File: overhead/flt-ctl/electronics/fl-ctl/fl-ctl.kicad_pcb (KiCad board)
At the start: 2 copper layers, 145 x 47.3 mm, 31 parts, among them J1 Conn_02x01, J2 Conn_02x05_Counter_Clockwise

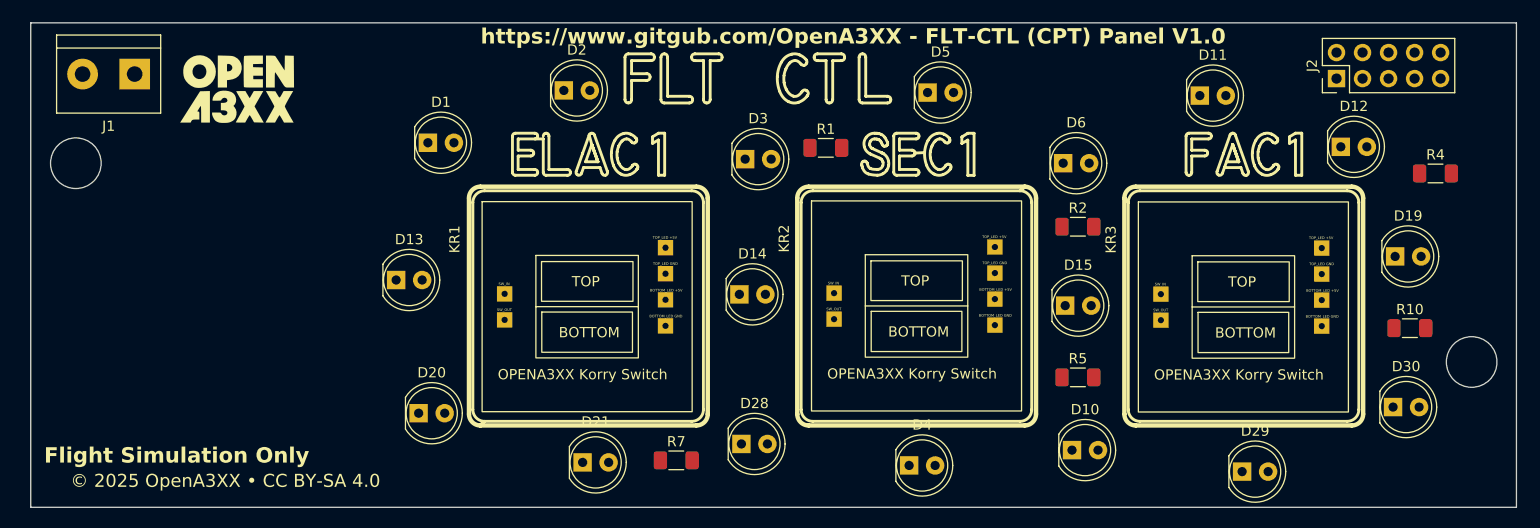
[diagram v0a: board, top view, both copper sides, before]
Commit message: Finalised ROuting for FLT-CTL CPT Side, and cleaned up ADIRS Panel PCB
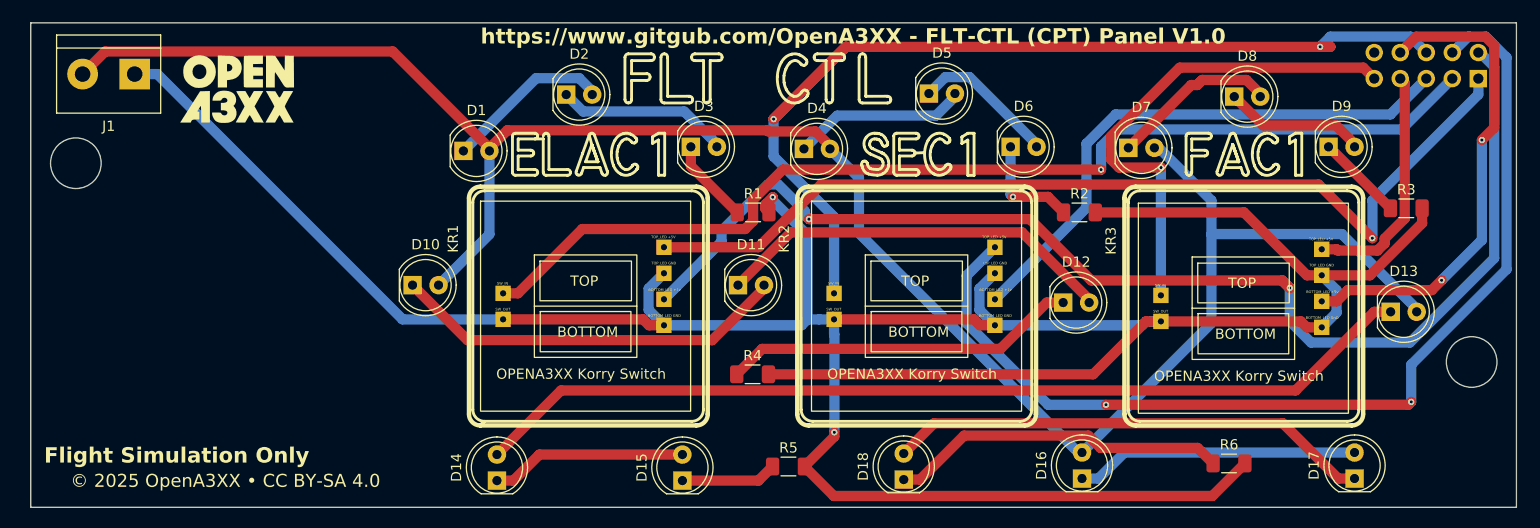
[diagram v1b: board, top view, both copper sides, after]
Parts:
- removed D19, D20, D21, D28, D29, D30: LED, LED_THT:LED_D5.0mm_Clear
- removed R10, R7: 220R, Resistor_SMD:R_1206_3216Metric_Pad1.30x1.75mm_HandSolder
- added D16: LED, LED_THT:LED_D5.0mm_Clear, F.Cu at (177.3, 121.4)
- added D17: LED, LED_THT:LED_D5.0mm_Clear, F.Cu at (203.9, 121.4)
- added D18: LED, LED_THT:LED_D5.0mm_Clear, F.Cu at (159.9, 121.5)
- added D7: LED, LED_THT:LED_D5.0mm_Clear, F.Cu at (181.8, 89.1)
- added D8: LED, LED_THT:LED_D5.0mm_Clear, F.Cu at (192.2, 84.1)
- added D9: LED, LED_THT:LED_D5.0mm_Clear, F.Cu at (201.4, 89.0)
- added R3: 220R, Resistor_SMD:R_1206_3216Metric_Pad1.30x1.75mm_HandSolder, F.Cu at (208.9, 95.0)
- added R6: 220R, Resistor_SMD:R_1206_3216Metric_Pad1.30x1.75mm_HandSolder, F.Cu at (191.7, 119.9)
- J2: moved to B.Cu
- moved D13 97.1 mm to (207.4, 105.1)
- moved R4 69.5 mm to (145.2, 111.2)
- moved D10 66.3 mm to (112.0, 102.5)
- moved D11 48.7 mm to (143.7, 102.5)
- moved D15 41.1 mm to (138.3, 121.6), turned to 90 degrees
- moved D4 32.6 mm to (150.2, 89.2)
- moved D12 31.1 mm to (175.5, 104.2)
- moved D14 29.8 mm to (120.2, 121.6), turned to 90 degrees
- moved R5 29.6 mm to (148.7, 120.2)
- moved J2 13.8 mm to (216.0, 82.3)
- moved R1 9.49 mm to (145.2, 95.4)
- moved D3 5.43 mm to (139.1, 89.0)
- moved D6 5.38 mm to (170.3, 89.0)
- moved D1 3.56 mm to (116.9, 89.4)
- moved R2 1.41 mm to (177.1, 95.4)
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- renumbered G*** to LogoBottom, G*** to LogoTop
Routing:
- net GND: track 0.00 -> 300.6 mm, vias 0 -> 2
- net +12V: track 0.00 -> 195.7 mm
- net Net-(J2-Pin_6): track 0.00 -> 131.0 mm, vias 0 -> 2
- net Net-(J2-Pin_2): track 0.00 -> 123.2 mm, vias 0 -> 2
- net Net-(J2-Pin_3): track 0.00 -> 103.9 mm, vias 0 -> 1
- net Net-(J2-Pin_4): track 0.00 -> 99.6 mm, vias 0 -> 2
- net Net-(J2-Pin_1): track 0.00 -> 93.7 mm, vias 0 -> 1
- net Net-(D13-K): track 0.00 -> 93.0 mm
- net Net-(J2-Pin_5): track 0.00 -> 54.7 mm
- net Net-(J2-Pin_9): track 0.00 -> 48.8 mm, vias 0 -> 1
- net Net-(J2-Pin_8): track 0.00 -> 47.8 mm, vias 0 -> 2
- net Net-(D17-K): track 0.00 -> 47.5 mm
- net Net-(D11-K): track 0.00 -> 39.4 mm
- net Net-(D10-K): track 0.00 -> 38.9 mm
- net Net-(D12-K): track 0.00 -> 34.8 mm
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
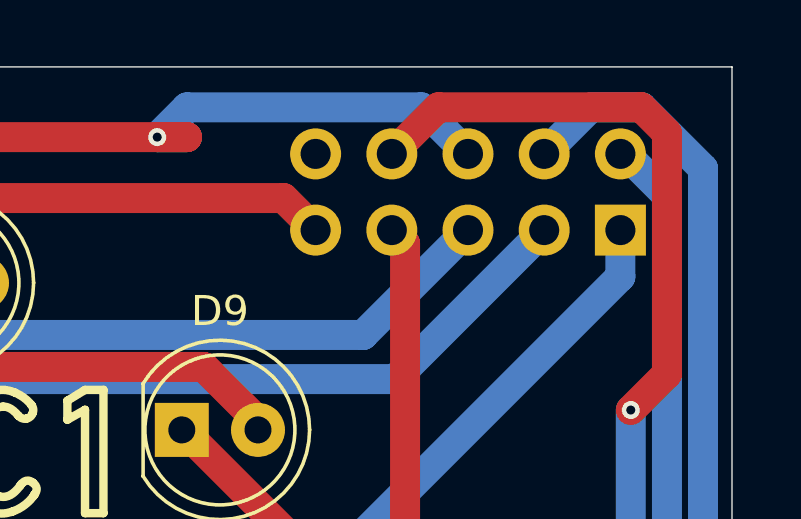
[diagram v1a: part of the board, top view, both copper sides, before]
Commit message: Completed markings for FL-CTL CPT SIDE - Completed
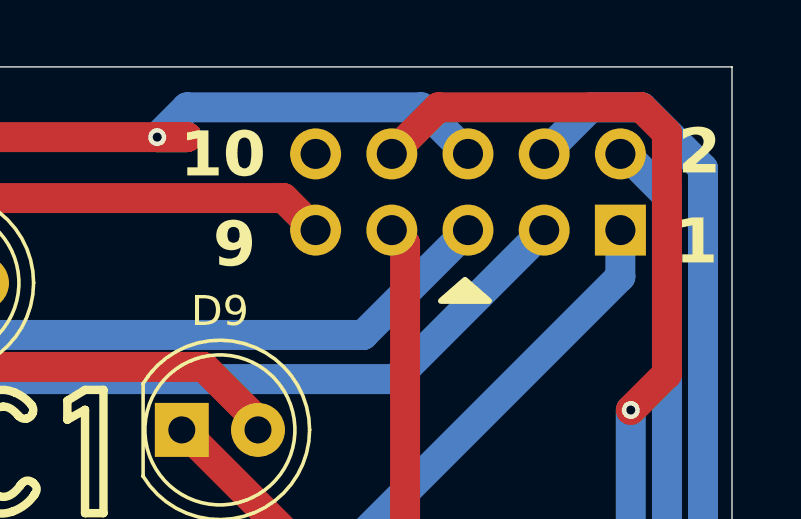
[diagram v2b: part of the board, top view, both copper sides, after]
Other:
- board text added: "+12V Variable Backlight"
- board text added: "1"
- board text added: "1-ELEC1-TOP_LED 2-ELEC1-BOTTOM_LED 3-ELEC1-KORRY_SW 4-SEC1-TOP_LED 5-SEC1-BOTTOM_LED 6-SEC1-KORRY_SW 7-FAC1-TOP_LED 8-FAC1-BOTTOM_LED 9-FAC1-KORRY_SW"
- board text added: "10"
- board text added: "2"
- board text added: "9"
- board text added: "GND"
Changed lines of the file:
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@@
 		(tags "Through hole pin header THT 2x05 2.54mm double row")
 		(property "Reference" "J2"
-			(at 1.27 2.38 270)
+			(at -2.66 1.12 0)
 			(layer "B.SilkS")
 			(effects
@@
 		(layer "F.SilkS")
 	)
+	(gr_poly
+		(pts
+			(xy 210 84.7) (xy 210.8 84) (xy 211.6 84.7)
+		)
+		(stroke
+			(width 0.2)
+			(type solid)
+		)
+		(fill yes)
+		(layer "F.SilkS")
+	)
 	(gr_curve
 		(pts
@@
 		(layer "B.SilkS")
 	)
+	(gr_poly
+		(pts
+			(xy 211.6 84.7) (xy 210.8 84) (xy 210 84.7)
+		)
+		(stroke
+			(width 0.2)
+			(type solid)
+		)
+		(fill yes)
+		(layer "B.SilkS")
+	)
 	(gr_line
 		(start 165.913777 89.228296)
@@
 		(layer "Edge.Cuts")
 	)
+	(gr_text "9"
+		(at 202.4 83.7 0)
+		(layer "F.SilkS")
+		(effects
+			(font
+				(size 1.5 1.5)
+				(thickness 0.3)
+				(bold yes)
+			)
+			(justify left bottom)
+		)
+	)
+	(gr_text "1"
+		(at 217.8 83.6 0)
+		(layer "F.SilkS")
+		(effects
+			(font
+				(size 1.5 1.5)
+				(thickness 0.3)
+				(bold yes)
+			)
+			(justify left bottom)
+		)
+	)
+	(gr_text "2"
+		(at 217.9 80.6 0)
+		(layer "F.SilkS")
+		(effects
+			(font
+				(size 1.5 1.5)
+				(thickness 0.3)
+				(bold yes)
+			)
+			(justify left bottom)
+		)
+	)
 	(gr_text "https://www.gitgub.com/OpenA3XX - FLT-CTL (CPT) Panel V1.0"
 		(at 118.6 79.1 0)
@@
 		)
 	)
+	(gr_text "10"
+		(at 201.3 80.7 0)
+		(layer "F.SilkS")
+		(effects
+			(font
+				(size 1.5 1.5)
+				(thickness 0.3)
+				(bold yes)
+			)
+			(justify left bottom)
+		)
+	)
+	(gr_text "1"
+		(at 219.5 83.6 -0)
+		(layer "B.SilkS")
+		(effects
+			(font
+				(size 1.5 1.5)
+				(thickness 0.3)
+				(bold yes)
+			)
+			(justify left bottom mirror)
+		)
+	)
 	(gr_text "Flight Simulation Only"
 		(at 101.9 119.8 0)
@@
 		)
 	)
+	(gr_text "10"
+		(at 204.4 80.7 -0)
+		(layer "B.SilkS")
+		(effects
+			(font
+				(size 1.5 1.5)
+				(thickness 0.3)
+				(bold yes)
+			)
+			(justify left bottom mirror)
+		)
+	)
 	(gr_text "https://www.gitgub.com/OpenA3XX - FLT-CTL (CPT) Panel V1.0"
 		(at 193 80.1 0)
@@
 		)
 	)
+	(gr_text "9"
+		(at 204.1 83.7 -0)
+		(layer "B.SilkS")
+		(effects
+			(font
+				(size 1.5 1.5)
+				(thickness 0.3)
+				(bold yes)
+			)
+			(justify left bottom mirror)
+		)
+	)
+	(gr_text "2"
+		(at 219.6 80.6 -0)
+		(layer "B.SilkS")
+		(effects
+			(font
+				(size 1.5 1.5)
+				(thickness 0.3)
+				(bold yes)
+			)
+			(justify left bottom mirror)
+		)
+	)
+	(gr_text "1-ELEC1-TOP_LED\n2-ELEC1-BOTTOM_LED\n3-ELEC1-KORRY_SW\n4-SEC1-TOP_LED\n5-SEC1-BOTTOM_LED\n6-SEC1-KORRY_SW\n7-FAC1-TOP_LED\n8-FAC1-BOTTOM_LED\n9-FAC1-KORRY_SW"
+		(at 214.9 92.2 -0)
+		(layer "B.SilkS")
+		(effects
+			(font
+				(size 0.5 0.5)
+				(thickness 0.125)
+				(bold yes)
+			)
+			(justify left bottom mirror)
+		)
+	)
+	(gr_text "+12V \nVariable Backlight"
+		(at 78.5 86.9 -0)
+		(layer "B.SilkS")
+		(effects
+			(font
+				(size 0.4 0.4)
+				(thickness 0.0625)
+			)
+			(justify mirror)
+		)
+	)
+	(gr_text "GND"
+		(at 84.8 86.9 -0)
+		(layer "B.SilkS")
+		(effects
+			(font
+				(size 0.4 0.4)
+				(thickness 0.0625)
+			)
+			(justify mirror)
+		)
+	)
